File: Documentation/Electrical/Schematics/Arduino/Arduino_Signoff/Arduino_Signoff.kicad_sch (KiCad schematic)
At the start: 11 parts, among them IC1 ATMEGA2560-15AU

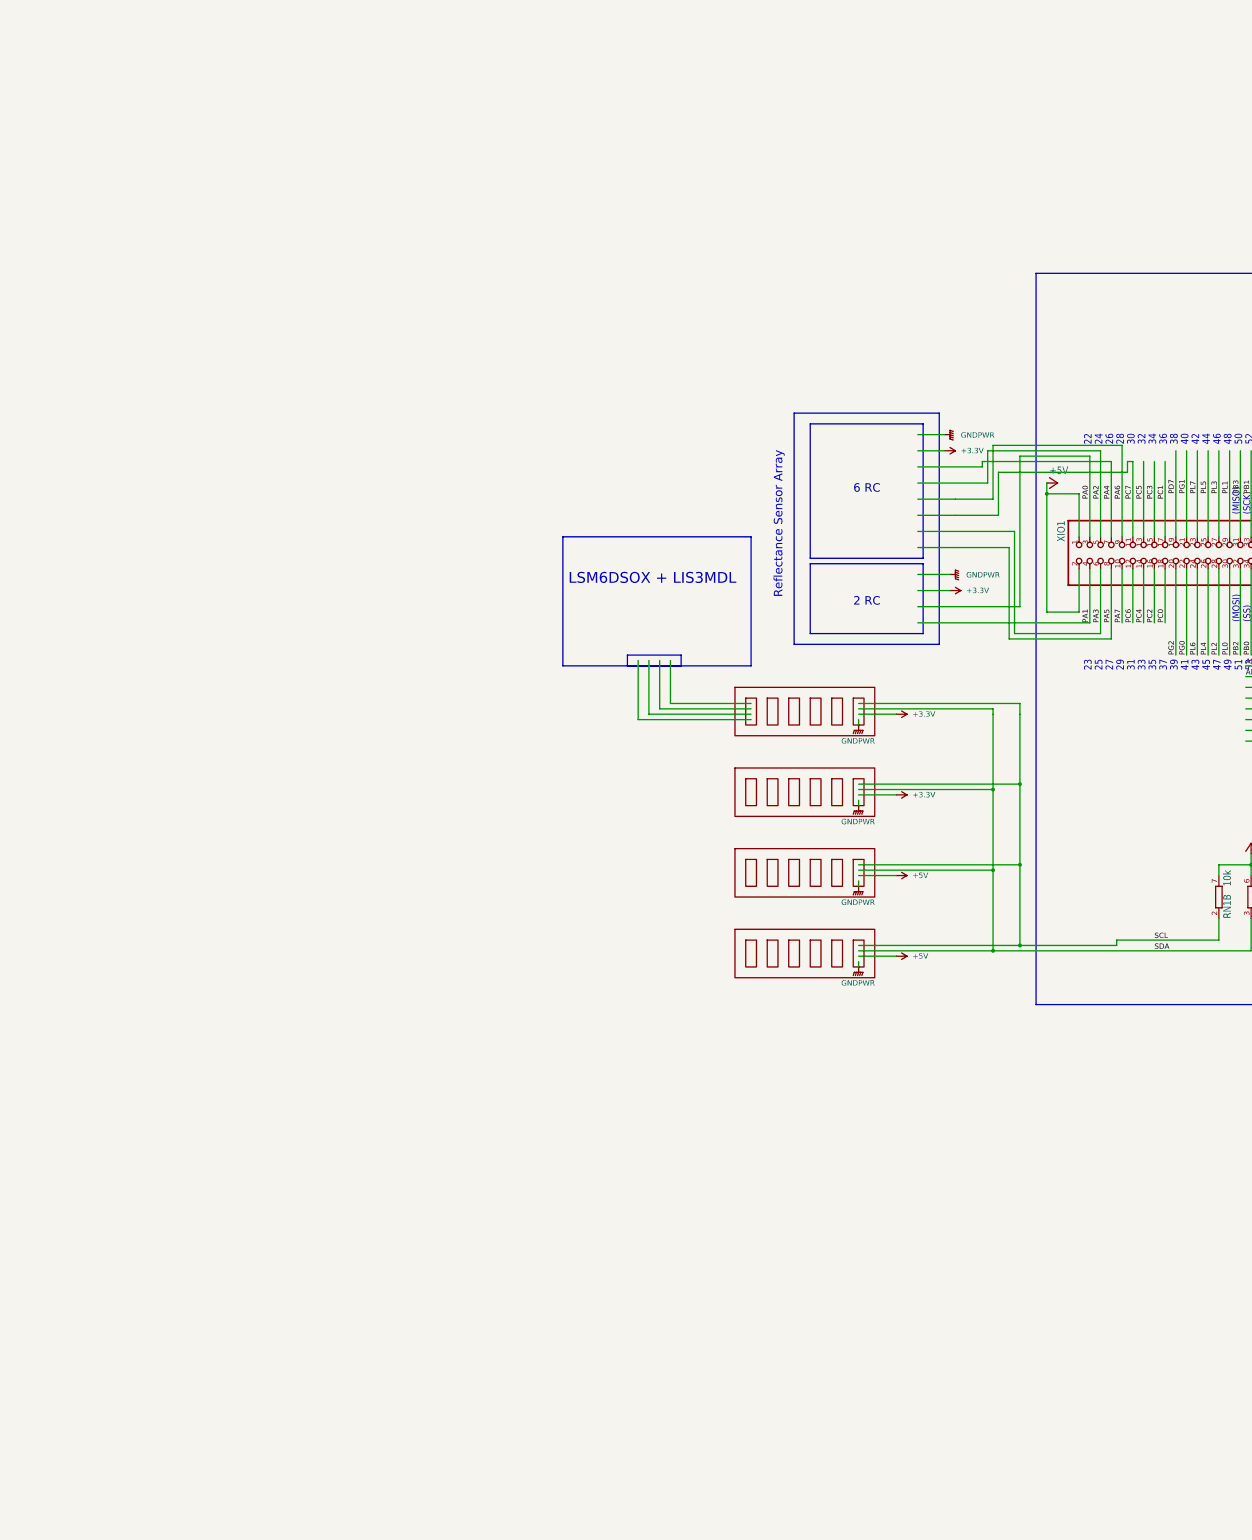
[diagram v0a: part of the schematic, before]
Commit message: Add reidcrews ObjDetect and Location sensors to Arduino Schematic
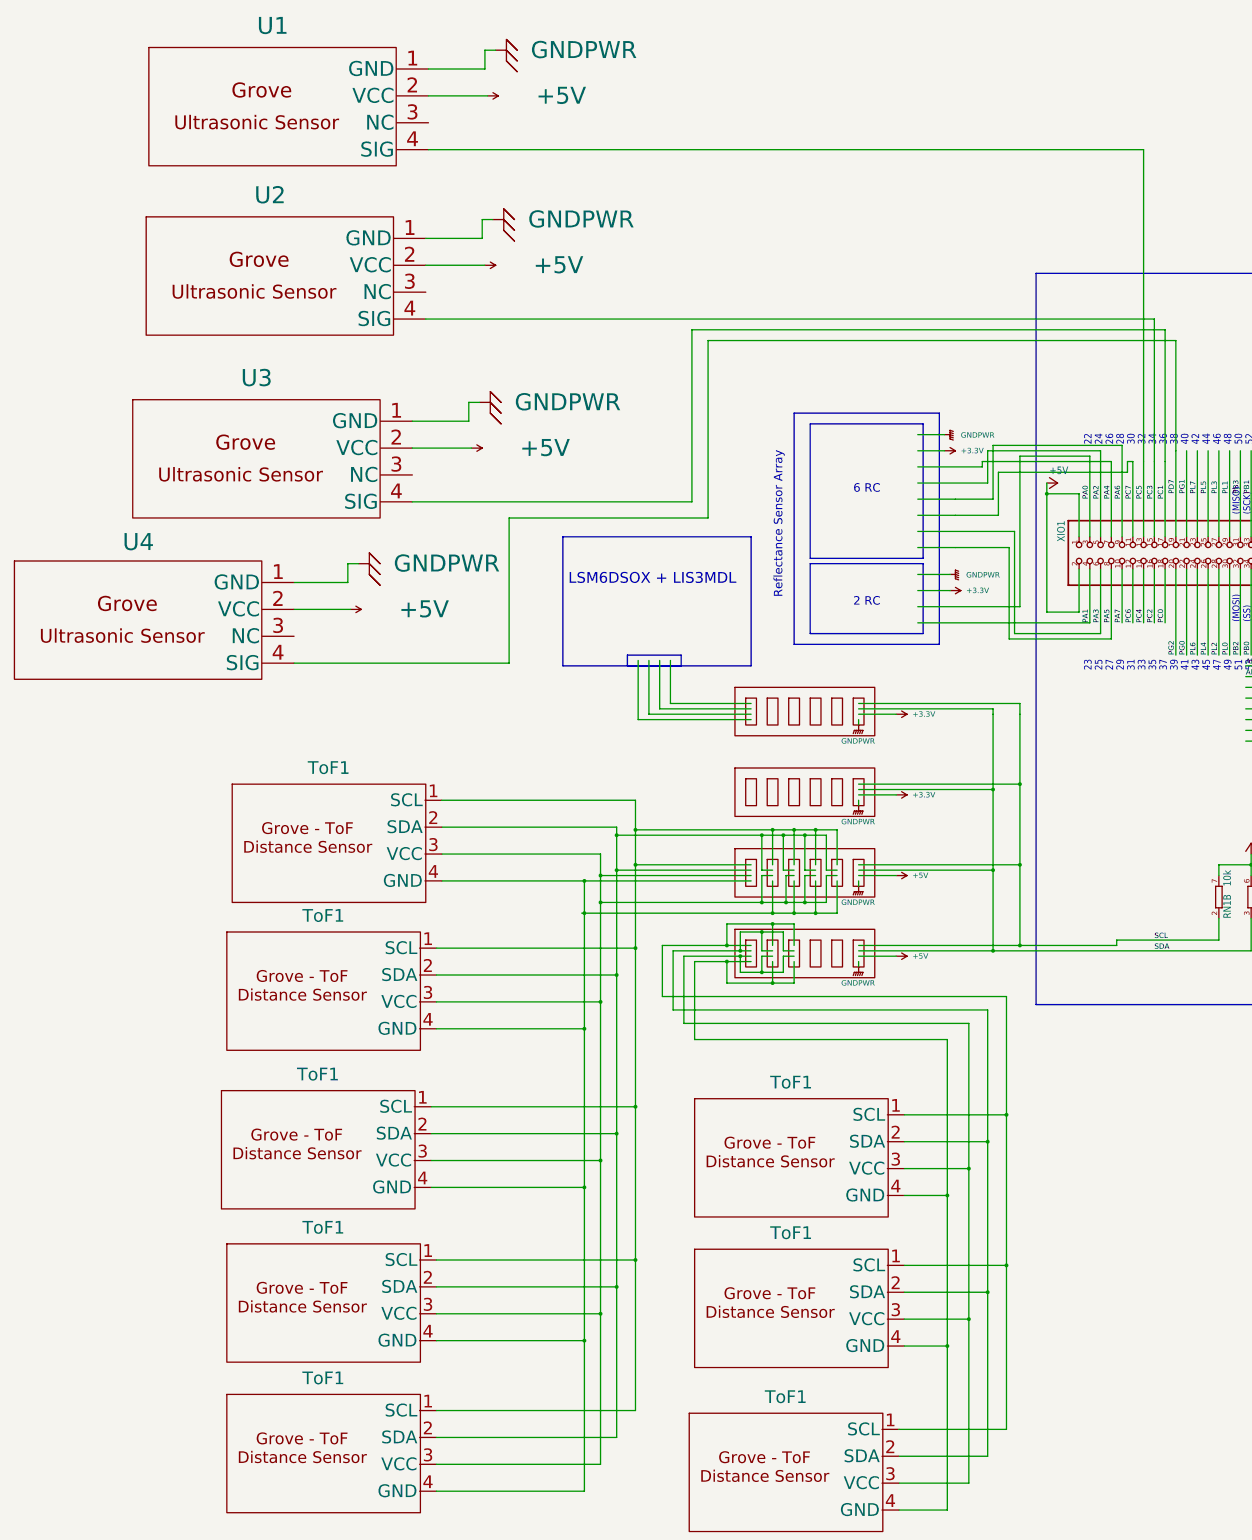
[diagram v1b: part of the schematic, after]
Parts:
- added ToF1 (x8): ~, symbol Time of Flight Sensor:Grove_-_Time_of_Flight_Distance_Sensor(VL53L0X)
- added U1, U2, U3, U4: ~, symbol UltrasonicSensor:SKU_101020010
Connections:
- net +3.3V: now also U1.2 (VCC), U2.2 (VCC), U3.2 (VCC), U4.2 (VCC)
- net GNDPWR: now also U1.1 (GND), U2.1 (GND), U3.1 (GND), U4.1 (GND)
- net PC1: now also U3.4 (SIG)
- net PC3: now also U2.4 (SIG)
- net PC5: now also U1.4 (SIG)
- net PD7: now also U4.4 (SIG)
- new net: ToF1.1 (SCL), ToF1.1 (SCL), ToF1.1 (SCL), ToF1.1 (SCL), ToF1.1 (SCL)
- new net: ToF1.2 (SDA), ToF1.2 (SDA), ToF1.2 (SDA), ToF1.2 (SDA), ToF1.2 (SDA)
- new net: ToF1.3 (VCC), ToF1.3 (VCC), ToF1.3 (VCC), ToF1.3 (VCC), ToF1.3 (VCC)
- new net: ToF1.4 (GND), ToF1.4 (GND), ToF1.4 (GND), ToF1.4 (GND), ToF1.4 (GND)
- new net: ToF1.1 (SCL), ToF1.1 (SCL), ToF1.1 (SCL)
- new net: ToF1.2 (SDA), ToF1.2 (SDA), ToF1.2 (SDA)
- new net: ToF1.3 (VCC), ToF1.3 (VCC), ToF1.3 (VCC)
- new net: ToF1.4 (GND), ToF1.4 (GND), ToF1.4 (GND)
